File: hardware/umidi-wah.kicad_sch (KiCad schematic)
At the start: 84 parts

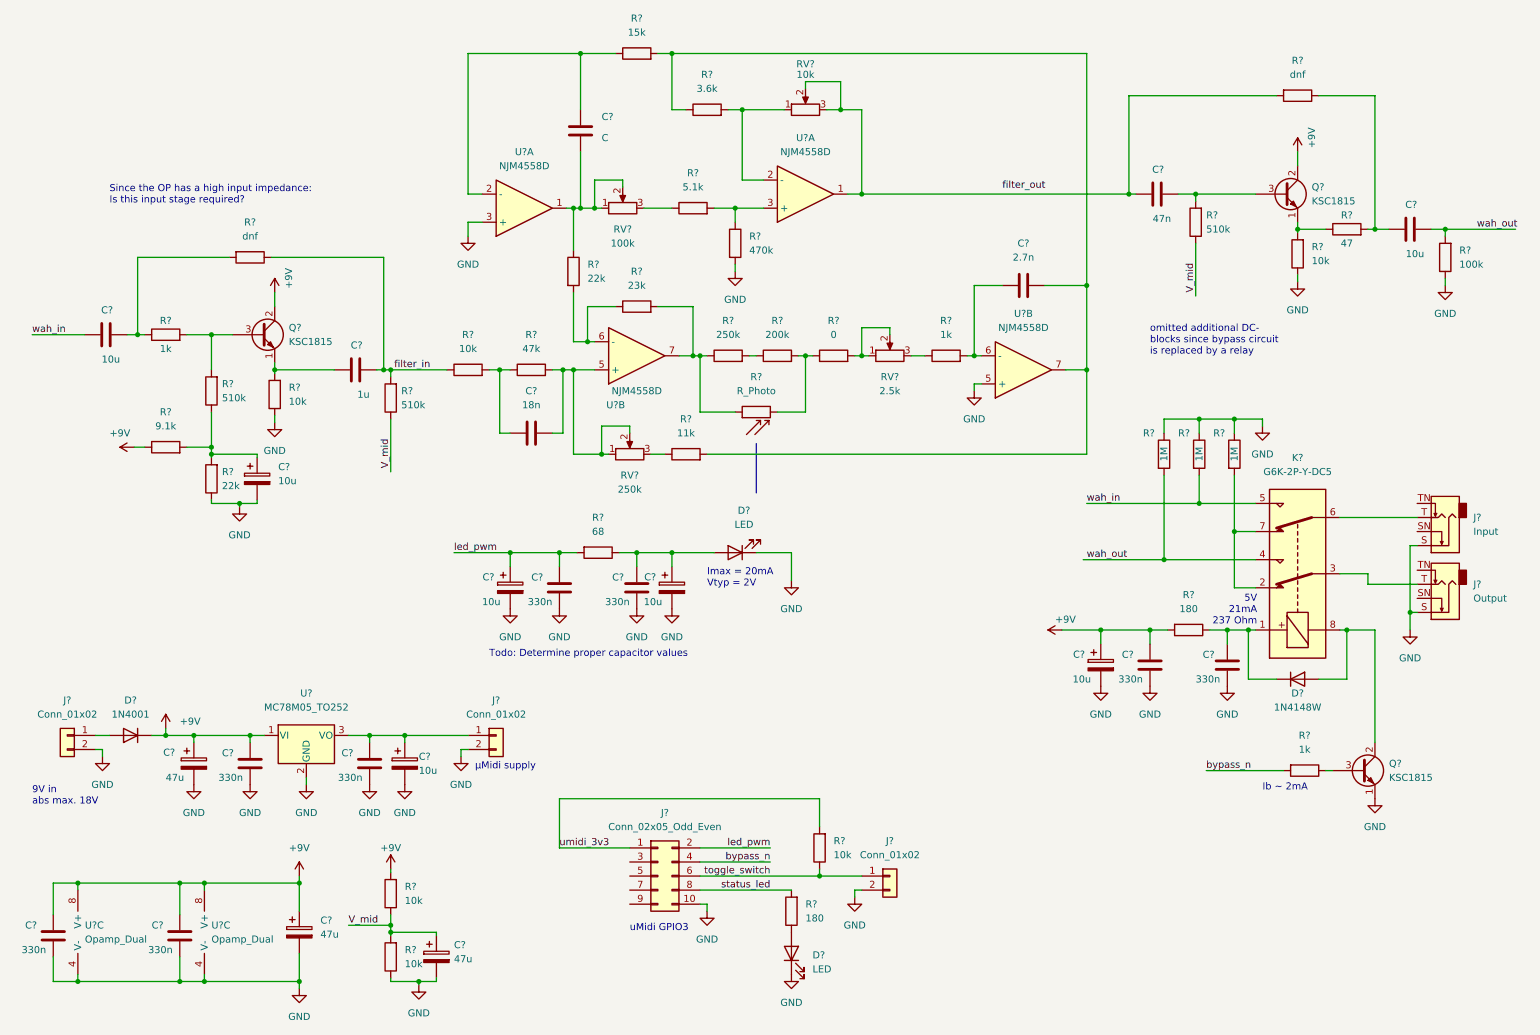
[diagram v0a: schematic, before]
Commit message: Convert led filter to T-type
Use the same values for the caps as used in our prototype. Use 2x 68 ohms instead of 2x 100 ohms, since this still results in a quiet low led current (10mA)
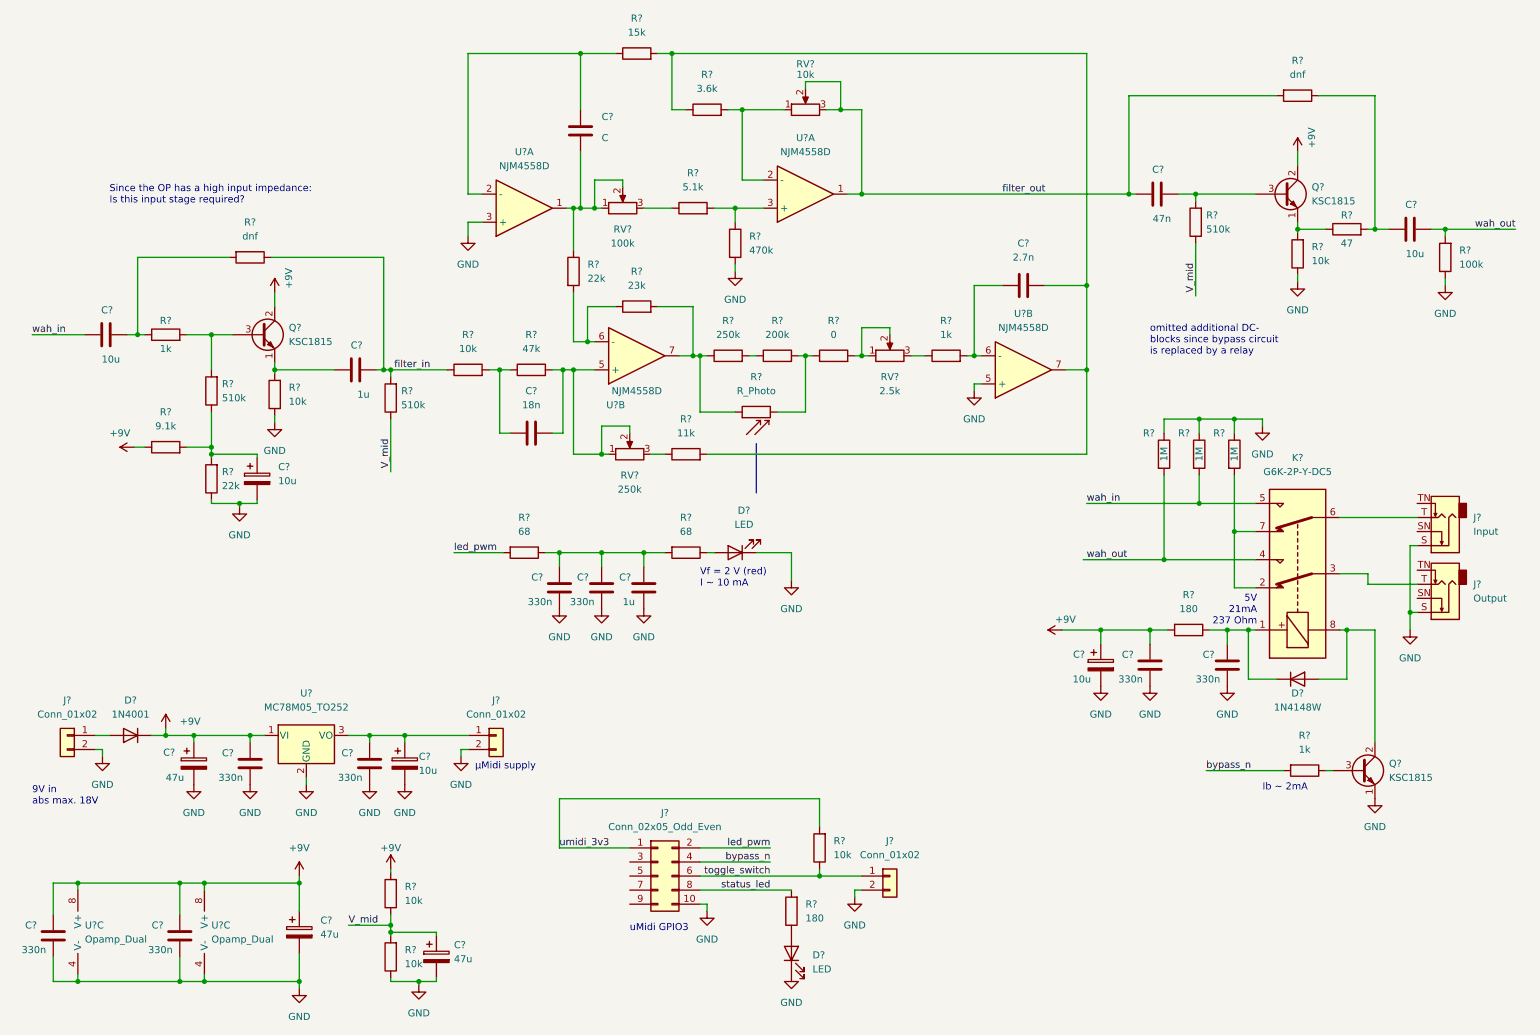
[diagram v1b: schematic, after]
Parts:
- removed C? (x2): 10u, symbol Device:C_Polarized
- added C?: 1u, symbol Device:C
- added R?: 68, symbol Device:R
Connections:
- net GND: now also C?.2
- net filter_out: now also C?.1, R?.2, RV?.2, RV?.3, U?.1
- net led_pwm: no longer C?.1
- net at C?.1, R?.1: now also C?.1, C?.1, R?.2; no longer D?.2 (A)
- new net: D?.2 (A), R?.1
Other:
- note added: "Vf = 2 V (red) I ~ 10 mA"
- note removed: "Imax = 20mA Vtyp = 2V"
- note removed: "Todo: Determine proper capacitor values"
- moved on the sheet: C?, R?

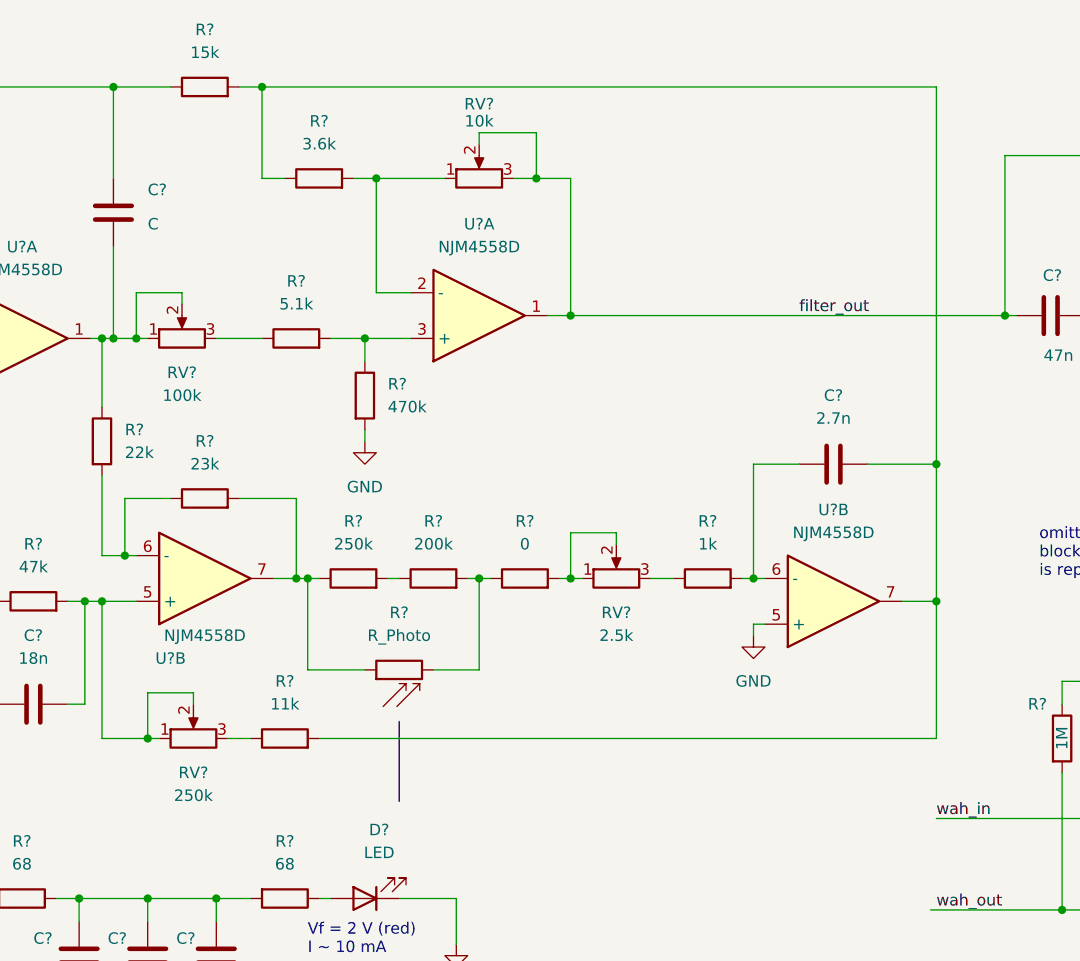
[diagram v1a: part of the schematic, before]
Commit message: Add/show potentiometer function fields
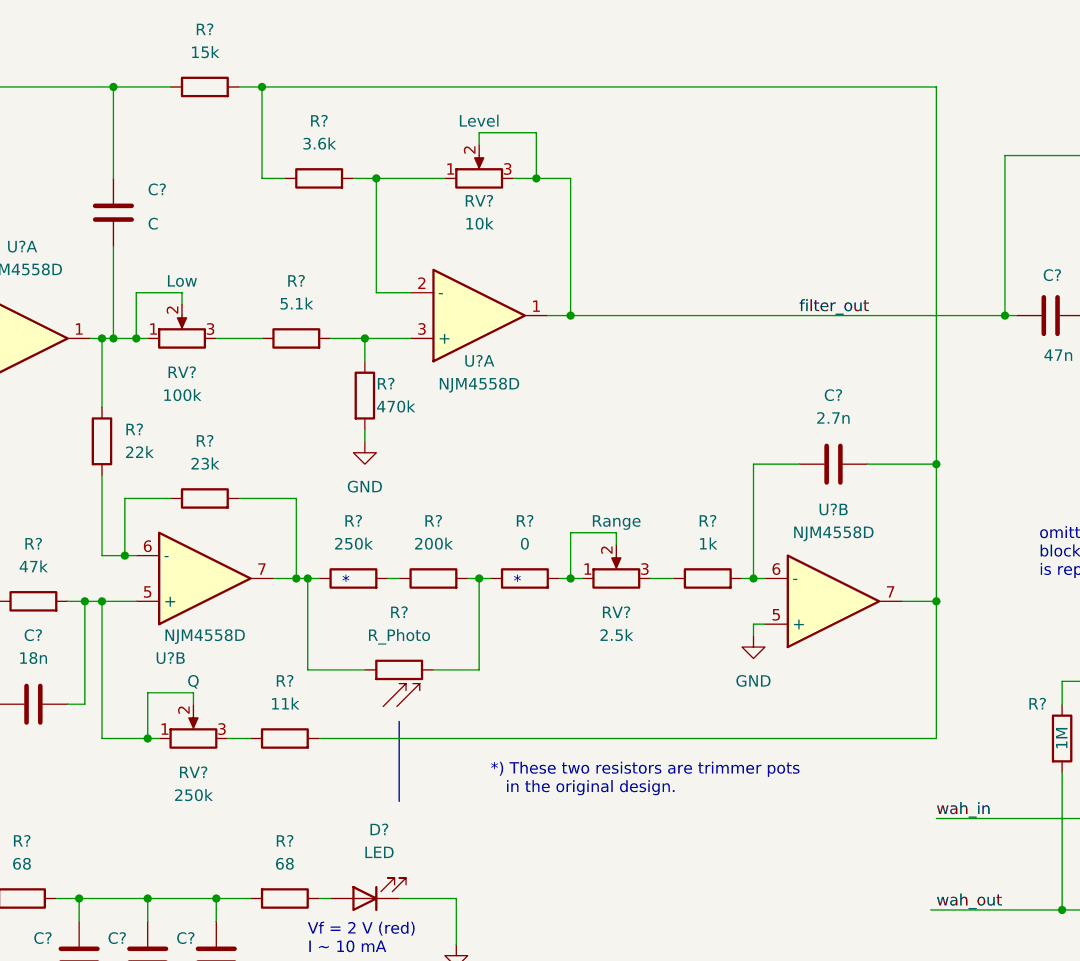
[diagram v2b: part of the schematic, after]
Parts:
- RV?: Function (none) -> Low
- RV?: Function (none) -> Range
- RV?: Function (none) -> Level
- RV?: Function (none) -> Q
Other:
- note added: "*"
- note added: "*) These two resistors are trimmer pots in the original design."
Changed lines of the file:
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@@
     (stroke (width 0) (type default) (color 0 0 0 0))
+  )
+  (text "*" (at 139.7 78.74 0)
+    (effects (font (size 1.27 1.27)) (justify left bottom))
   )
   (text "9V in\nabs max. 18V" (at 15.24 158.75 0)
@@
     (effects (font (size 1.27 1.27)) (justify left bottom))
   )
+  (text "*" (at 158.75 78.74 0)
+    (effects (font (size 1.27 1.27)) (justify left bottom))
+  )
   (text "uMidi GPIO3" (at 123.19 181.61 0)
+    (effects (font (size 1.27 1.27)) (justify left bottom))
+  )
+  (text "*) These two resistors are trimmer pots\n   in the original design."
+    (at 156.21 101.6 0)
     (effects (font (size 1.27 1.27)) (justify left bottom))
   )
@@
   )
   (symbol (lib_id "Device:R_Potentiometer") (at 121.92 50.8 90) (unit 1)
-    (in_bom yes) (on_board yes) (fields_autoplaced)
+    (in_bom yes) (on_board yes)
     (property "Reference" "RV?" (id 0) (at 121.92 54.61 90))
     (property "Value" "100k" (id 1) (at 121.92 57.15 90))
@@
       (effects (font (size 1.27 1.27)) hide)
     )
+    (property "Function" "Low" (id 4) (at 121.92 44.45 90))
     (pin "1")
     (pin "2")
@@
   )
   (symbol (lib_id "Device:Opamp_Dual") (at 154.94 48.26 0) (mirror x) (unit 1)
-    (in_bom yes) (on_board yes) (fields_autoplaced)
-    (property "Reference" "U?" (id 0) (at 154.94 38.1 0))
-    (property "Value" "NJM4558D" (id 1) (at 154.94 40.64 0))
+    (in_bom yes) (on_board yes)
+    (property "Reference" "U?" (id 0) (at 154.94 53.34 0))
+    (property "Value" "NJM4558D" (id 1) (at 154.94 55.88 0))
     (property "Footprint" "" (id 2) (at 154.94 48.26 0)
       (effects (font (size 1.27 1.27)) hide)
@@
   )
   (symbol (lib_id "Device:R_Potentiometer") (at 170.18 77.47 90) (unit 1)
-    (in_bom yes) (on_board yes) (fields_autoplaced)
+    (in_bom yes) (on_board yes)
     (property "Reference" "RV?" (id 0) (at 170.18 81.28 90))
     (property "Value" "2.5k" (id 1) (at 170.18 83.82 90))
@@
       (effects (font (size 1.27 1.27)) hide)
     )
+    (property "Function" "Range" (id 4) (at 170.18 71.12 90))
     (pin "1")
     (pin "2")
@@
   )
   (symbol (lib_id "Device:R") (at 142.24 57.15 0) (unit 1)
-    (in_bom yes) (on_board yes) (fields_autoplaced)
-    (property "Reference" "R?" (id 0) (at 144.78 55.8799 0)
-      (effects (font (size 1.27 1.27)) (justify left))
-    )
-    (property "Value" "470k" (id 1) (at 144.78 58.4199 0)
+    (in_bom yes) (on_board yes)
+    (property "Reference" "R?" (id 0) (at 143.51 55.88 0)
+      (effects (font (size 1.27 1.27)) (justify left))
+    )
+    (property "Value" "470k" (id 1) (at 143.51 58.42 0)
       (effects (font (size 1.27 1.27)) (justify left))
     )
@@
   (symbol (lib_id "Device:R_Potentiometer") (at 154.94 33.02 90) (unit 1)
     (in_bom yes) (on_board yes)
-    (property "Reference" "RV?" (id 0) (at 154.94 24.765 90))
-    (property "Value" "10k" (id 1) (at 154.94 26.67 90))
+    (property "Reference" "RV?" (id 0) (at 154.94 35.56 90))
+    (property "Value" "10k" (id 1) (at 154.94 38.1 90))
     (property "Footprint" "" (id 2) (at 154.94 33.02 0)
       (effects (font (size 1.27 1.27)) hide)
@@
       (effects (font (size 1.27 1.27)) hide)
     )
+    (property "Function" "Level" (id 4) (at 154.94 26.67 90))
     (pin "1")
     (pin "2")
@@
   )
   (symbol (lib_id "Device:R_Potentiometer") (at 123.19 95.25 90) (unit 1)
-    (in_bom yes) (on_board yes) (fields_autoplaced)
+    (in_bom yes) (on_board yes)
     (property "Reference" "RV?" (id 0) (at 123.19 99.06 90))
     (property "Value" "250k" (id 1) (at 123.19 101.6 90))
@@
       (effects (font (size 1.27 1.27)) hide)
     )
-    (pin "1")
-    (pin "2")
+    (property "Function" "Q" (id 4) (at 123.19 88.9 90))
+    (pin "1")
+    (pin "2")

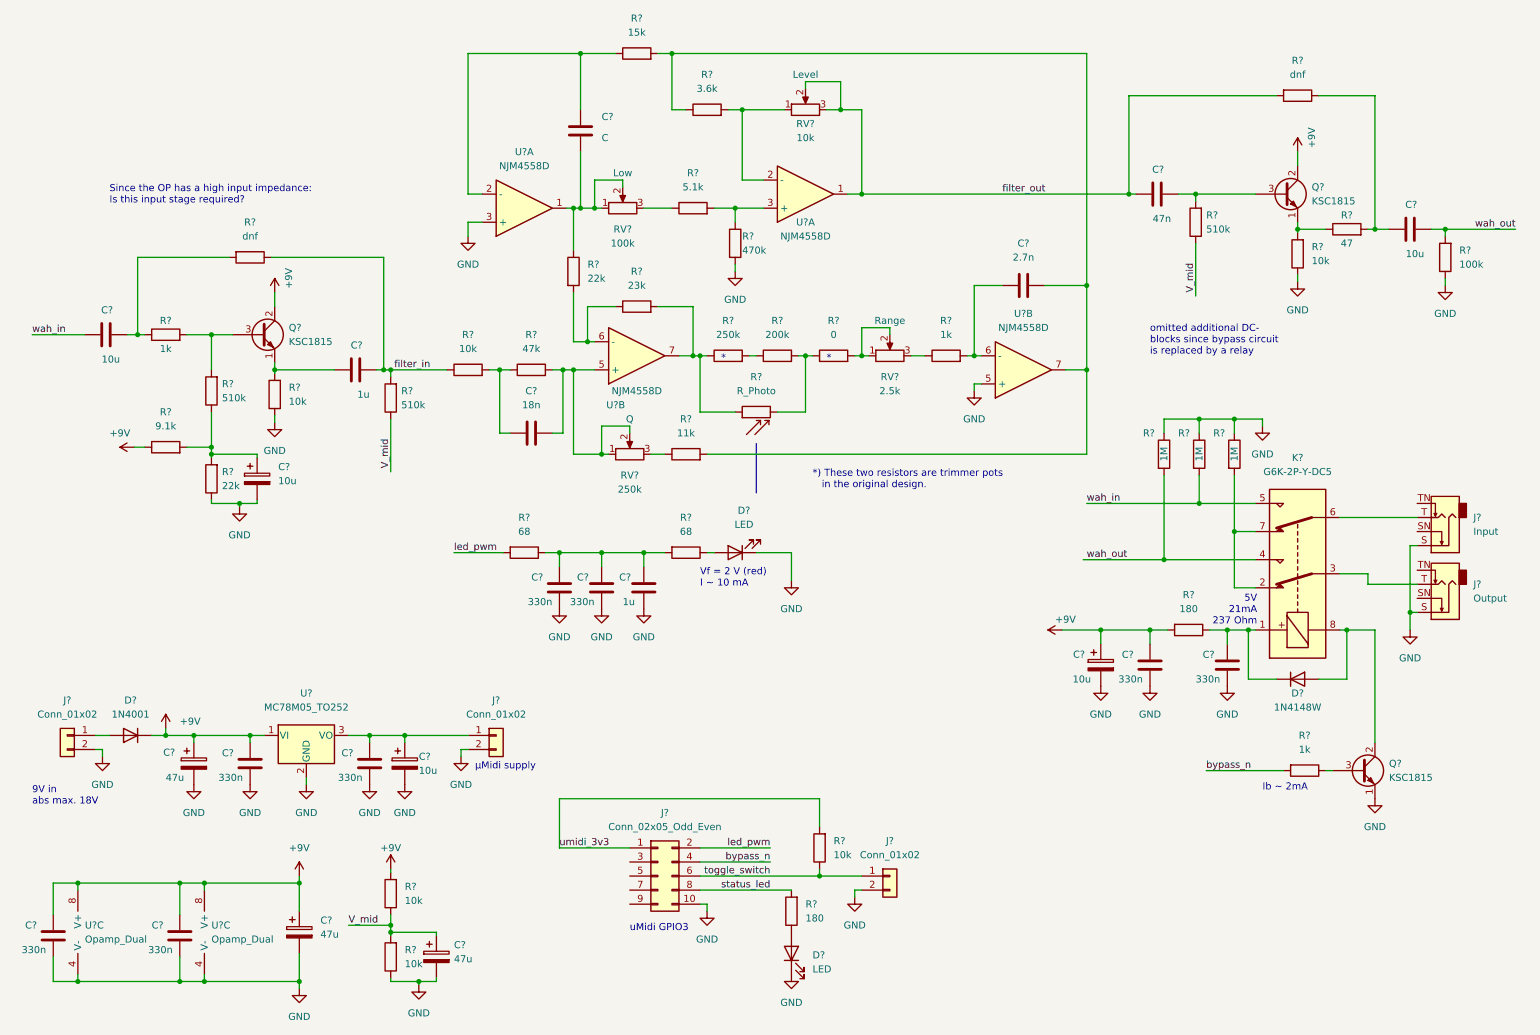
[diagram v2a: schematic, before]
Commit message: Annotate schematic, assign footprints for jacks
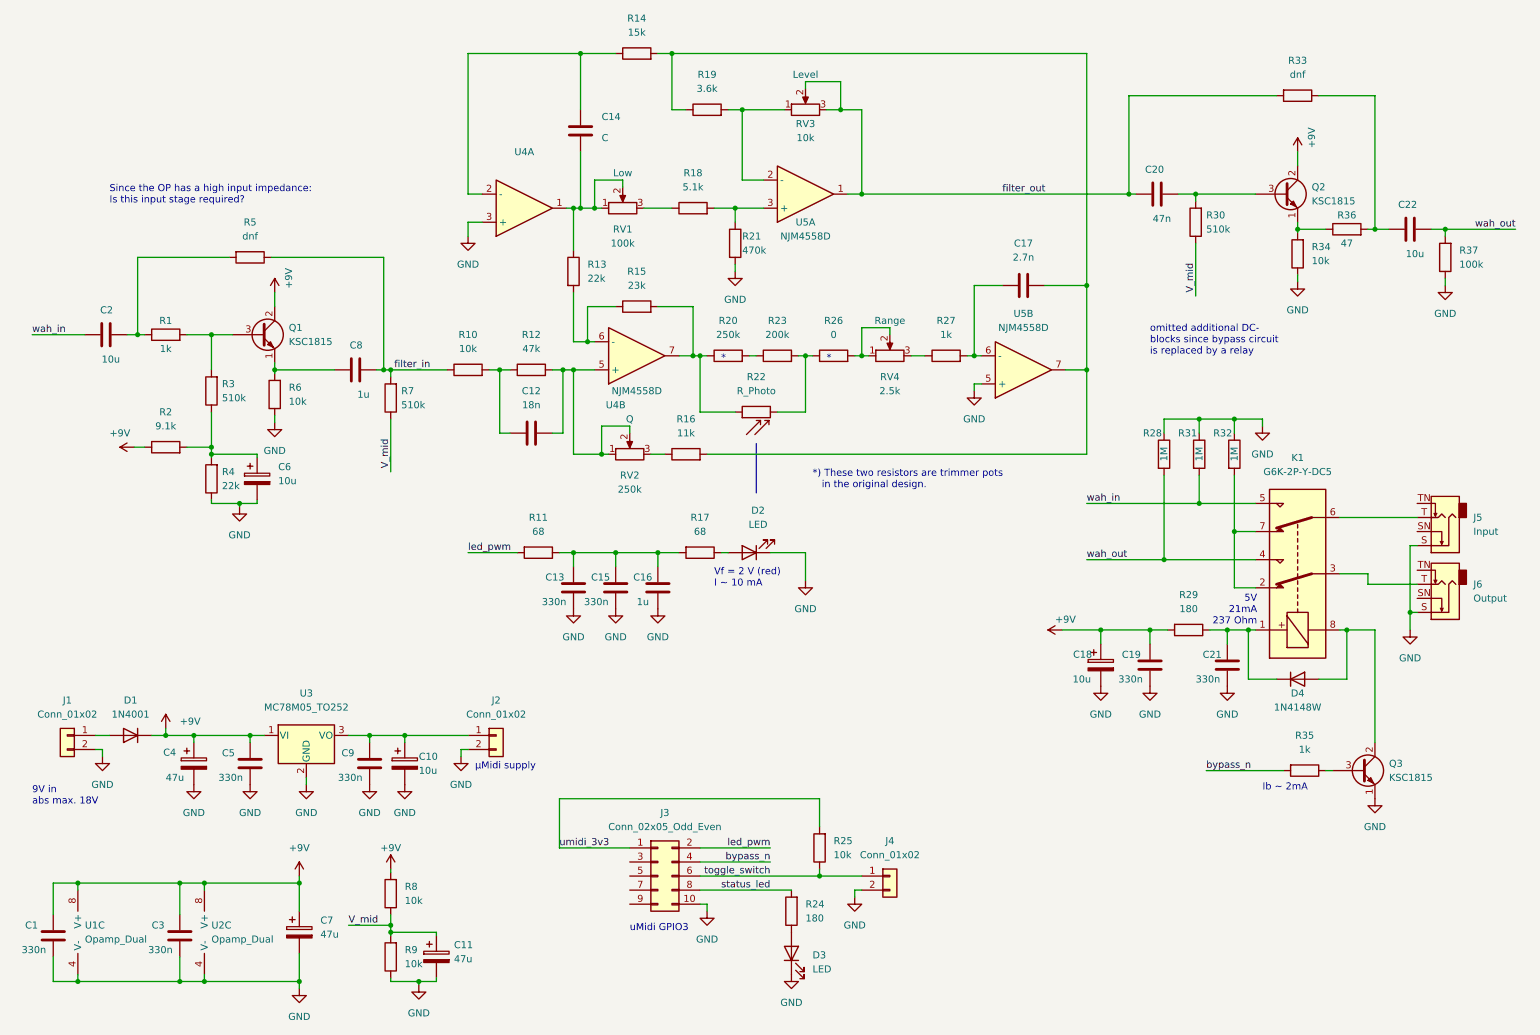
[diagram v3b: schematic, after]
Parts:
- J5, J6: renamed from J?; footprint (none) -> Connector_Audio:Jack_6.35mm_Neutrik_NMJ4HCD2_Horizontal
- K1: renamed from K?; footprint (none) -> Relay_THT:Relay_DPDT_Omron_G6K-2P-Y
- U4, U5: renamed from U?; footprint (none) -> Package_DIP:DIP-8_W7.62mm_Socket_LongPads
- gave numbers to parts that had none: 78
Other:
- moved on the sheet: C13, C15, C16, D2, R11, R17
